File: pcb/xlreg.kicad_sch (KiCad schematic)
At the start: 12 parts, among them Q1076 2N7002a, Q1077 2N7002a, Q1078 2N7002a, Q1079 2N7002a, Q1080 2N7002a, Q1081 2N7002a, Q1082 2N7002a, Q1083 2N7002a, Q1084 2N7002a, Q1085 2N7002a

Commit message: XH/XL.
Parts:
- renumbered Q1076 to Q1009, Q1077 to Q1010, Q1078 to Q1011, Q1079 to Q1012, Q1080 to Q1013, Q1081 to Q1014, Q1082 to Q1015, Q1083 to Q1016, Q1084 to Q1017, Q1085 to Q1018, R466 to R441, R467 to R442
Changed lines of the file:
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@@
     (effects (font (size 1.27 1.27)) (justify left))
   )
-  (symbol (lib_id "power:VCC") (at 67.31 104.14 0) (unit 1)
-    (in_bom yes) (on_board yes)
-    (property "Reference" "#PWR0981" (id 0) (at 67.31 107.95 0)
+  (symbol (lib_id "power:VCC") (at 67.31 104.14 0)
+    (in_bom yes) (on_board yes)
+    (property "Reference" "#PWR0930" (id 0) (at 67.31 107.95 0)
       (effects (font (size 1.27 1.27)) hide)
     )
@@
     (pin "1")
   )
-  (symbol (lib_id "power:VCC") (at 135.89 46.99 0) (unit 1)
-    (in_bom yes) (on_board yes)
-    (property "Reference" "#PWR0973" (id 0) (at 135.89 50.8 0)
+  (symbol (lib_id "power:VCC") (at 135.89 46.99 0)
+    (in_bom yes) (on_board yes)
+    (property "Reference" "#PWR0922" (id 0) (at 135.89 50.8 0)
       (effects (font (size 1.27 1.27)) hide)
     )
@@
     (pin "1")
   )
-  (symbol (lib_id "power:GND") (at 67.31 87.63 0) (unit 1)
-    (in_bom yes) (on_board yes)
-    (property "Reference" "#PWR0976" (id 0) (at 67.31 93.98 0)
+  (symbol (lib_id "power:GND") (at 67.31 87.63 0)
+    (in_bom yes) (on_board yes)
+    (property "Reference" "#PWR0925" (id 0) (at 67.31 93.98 0)
       (effects (font (size 1.27 1.27)) hide)
     )
@@
     (pin "1")
   )
-  (symbol (lib_id "power:GND") (at 67.31 130.81 0) (unit 1)
-    (in_bom yes) (on_board yes)
-    (property "Reference" "#PWR0982" (id 0) (at 67.31 137.16 0)
+  (symbol (lib_id "power:GND") (at 67.31 130.81 0)
+    (in_bom yes) (on_board yes)
+    (property "Reference" "#PWR0931" (id 0) (at 67.31 137.16 0)
       (effects (font (size 1.27 1.27)) hide)
     )
@@
     (pin "1")
   )
-  (symbol (lib_id "power:GND") (at 93.98 95.25 0) (unit 1)
-    (in_bom yes) (on_board yes)
-    (property "Reference" "#PWR0977" (id 0) (at 93.98 101.6 0)
+  (symbol (lib_id "power:GND") (at 93.98 95.25 0)
+    (in_bom yes) (on_board yes)
+    (property "Reference" "#PWR0926" (id 0) (at 93.98 101.6 0)
       (effects (font (size 1.27 1.27)) hide)
     )
@@
     (pin "1")
   )
-  (symbol (lib_id "power:GND") (at 119.38 96.52 0) (unit 1)
-    (in_bom yes) (on_board yes)
-    (property "Reference" "#PWR0979" (id 0) (at 119.38 102.87 0)
+  (symbol (lib_id "power:GND") (at 119.38 96.52 0)
+    (in_bom yes) (on_board yes)
+    (property "Reference" "#PWR0928" (id 0) (at 119.38 102.87 0)
       (effects (font (size 1.27 1.27)) hide)
     )
@@
     (pin "1")
   )
-  (symbol (lib_id "power:GND") (at 148.59 96.52 0) (unit 1)
-    (in_bom yes) (on_board yes)
-    (property "Reference" "#PWR0980" (id 0) (at 148.59 102.87 0)
+  (symbol (lib_id "power:GND") (at 148.59 96.52 0)
+    (in_bom yes) (on_board yes)
+    (property "Reference" "#PWR0929" (id 0) (at 148.59 102.87 0)
       (effects (font (size 1.27 1.27)) hide)
     )
@@
     (pin "1")
   )
-  (symbol (lib_id "power:GND") (at 205.74 63.5 90) (unit 1)
-    (in_bom yes) (on_board yes)
-    (property "Reference" "#PWR0974" (id 0) (at 212.09 63.5 0)
+  (symbol (lib_id "power:GND") (at 205.74 63.5 90)
+    (in_bom yes) (on_board yes)
+    (property "Reference" "#PWR0923" (id 0) (at 212.09 63.5 0)
       (effects (font (size 1.27 1.27)) hide)
     )
@@
     (pin "1")
   )
-  (symbol (lib_id "power:GND") (at 205.74 68.58 90) (unit 1)
-    (in_bom yes) (on_board yes)
-    (property "Reference" "#PWR0975" (id 0) (at 212.09 68.58 0)
+  (symbol (lib_id "power:GND") (at 205.74 68.58 90)
+    (in_bom yes) (on_board yes)
+    (property "Reference" "#PWR0924" (id 0) (at 212.09 68.58 0)
       (effects (font (size 1.27 1.27)) hide)
     )
@@
     (pin "1")
   )
-  (symbol (lib_id "power:GND") (at 240.03 95.25 0) (unit 1)
-    (in_bom yes) (on_board yes)
-    (property "Reference" "#PWR0978" (id 0) (at 240.03 101.6 0)
+  (symbol (lib_id "power:GND") (at 240.03 95.25 0)
+    (in_bom yes) (on_board yes)
+    (property "Reference" "#PWR0927" (id 0) (at 240.03 101.6 0)
       (effects (font (size 1.27 1.27)) hide)
     )
@@
     (pin "1")
   )
-  (symbol (lib_id "Device:R") (at 67.31 107.95 0) (unit 1)
-    (in_bom yes) (on_board yes)
-    (property "Reference" "R467" (id 0) (at 69.088 106.7816 0)
+  (symbol (lib_id "Device:R") (at 67.31 107.95 0)
+    (in_bom yes) (on_board yes)
+    (property "Reference" "R442" (id 0) (at 69.088 106.7816 0)
       (effects (font (size 1.27 1.27)) (justify left))
     )
@@
     (pin "2")
   )
-  (symbol (lib_id "Device:R") (at 135.89 50.8 0) (unit 1)
-    (in_bom yes) (on_board yes)
-    (property "Reference" "R466" (id 0) (at 137.668 49.6316 0)
+  (symbol (lib_id "Device:R") (at 135.89 50.8 0)
+    (in_bom yes) (on_board yes)
+    (property "Reference" "R441" (id 0) (at 137.668 49.6316 0)
       (effects (font (size 1.27 1.27)) (justify left))
     )
@@
     (pin "2")
   )
-  (symbol (lib_id "Transistor_FET:2N7002") (at 64.77 82.55 0) (unit 1)
-    (in_bom yes) (on_board yes)
-    (property "Reference" "Q1080" (id 0) (at 70.0024 81.3816 0)
+  (symbol (lib_id "Transistor_FET:2N7002") (at 64.77 82.55 0)
+    (in_bom yes) (on_board yes)
+    (property "Reference" "Q1013" (id 0) (at 70.0024 81.3816 0)
       (effects (font (size 1.27 1.27)) (justify left))
     )
@@
     (pin "3")
   )
-  (symbol (lib_id "Transistor_FET:2N7002") (at 64.77 125.73 0) (unit 1)
-    (in_bom yes) (on_board yes)
-    (property "Reference" "Q1085" (id 0) (at 70.0024 124.5616 0)
+  (symbol (lib_id "Transistor_FET:2N7002") (at 64.77 125.73 0)
+    (in_bom yes) (on_board yes)
+    (property "Reference" "Q1018" (id 0) (at 70.0024 124.5616 0)
       (effects (font (size 1.27 1.27)) (justify left))
     )
@@
     (pin "3")
   )
-  (symbol (lib_id "Transistor_FET:2N7002") (at 91.44 80.01 0) (unit 1)
-    (in_bom yes) (on_board yes)
-    (property "Reference" "Q1076" (id 0) (at 96.6724 78.8416 0)
+  (symbol (lib_id "Transistor_FET:2N7002") (at 91.44 80.01 0)
+    (in_bom yes) (on_board yes)
+    (property "Reference" "Q1009" (id 0) (at 96.6724 78.8416 0)
       (effects (font (size 1.27 1.27)) (justify left))
     )
@@
     (pin "3")
   )
-  (symbol (lib_id "Transistor_FET:2N7002") (at 91.44 90.17 0) (unit 1)
-    (in_bom yes) (on_board yes)
-    (property "Reference" "Q1081" (id 0) (at 96.6724 89.0016 0)
+  (symbol (lib_id "Transistor_FET:2N7002") (at 91.44 90.17 0)
+    (in_bom yes) (on_board yes)
+    (property "Reference" "Q1014" (id 0) (at 96.6724 89.0016 0)
       (effects (font (size 1.27 1.27)) (justify left))
     )
@@
     (pin "3")
   )
-  (symbol (lib_id "Transistor_FET:2N7002") (at 116.84 81.28 0) (unit 1)
-    (in_bom yes) (on_board yes)
-    (property "Reference" "Q1078" (id 0) (at 122.0724 80.1116 0)
+  (symbol (lib_id "Transistor_FET:2N7002") (at 116.84 81.28 0)
+    (in_bom yes) (on_board yes)
+    (property "Reference" "Q1011" (id 0) (at 122.0724 80.1116 0)
       (effects (font (size 1.27 1.27)) (justify left))
     )
@@
     (pin "3")
   )
-  (symbol (lib_id "Transistor_FET:2N7002") (at 116.84 91.44 0) (unit 1)
-    (in_bom yes) (on_board yes)
-    (property "Reference" "Q1083" (id 0) (at 122.0724 90.2716 0)
+  (symbol (lib_id "Transistor_FET:2N7002") (at 116.84 91.44 0)
+    (in_bom yes) (on_board yes)
+    (property "Reference" "Q1016" (id 0) (at 122.0724 90.2716 0)
       (effects (font (size 1.27 1.27)) (justify left))
     )
@@
     (pin "3")
   )
-  (symbol (lib_id "Transistor_FET:2N7002") (at 146.05 81.28 0) (unit 1)
-    (in_bom yes) (on_board yes)
-    (property "Reference" "Q1079" (id 0) (at 151.2824 80.1116 0)
+  (symbol (lib_id "Transistor_FET:2N7002") (at 146.05 81.28 0)
+    (in_bom yes) (on_board yes)
+    (property "Reference" "Q1012" (id 0) (at 151.2824 80.1116 0)
       (effects (font (size 1.27 1.27)) (justify left))
     )
@@
     (pin "3")
   )
-  (symbol (lib_id "Transistor_FET:2N7002") (at 146.05 91.44 0) (unit 1)
-    (in_bom yes) (on_board yes)
-    (property "Reference" "Q1084" (id 0) (at 151.2824 90.2716 0)
+  (symbol (lib_id "Transistor_FET:2N7002") (at 146.05 91.44 0)
+    (in_bom yes) (on_board yes)
+    (property "Reference" "Q1017" (id 0) (at 151.2824 90.2716 0)
       (effects (font (size 1.27 1.27)) (justify left))
     )
@@
     (pin "3")
   )
-  (symbol (lib_id "Transistor_FET:2N7002") (at 237.49 80.01 0) (unit 1)
-    (in_bom yes) (on_board yes)
-    (property "Reference" "Q1077" (id 0) (at 242.7224 78.8416 0)
+  (symbol (lib_id "Transistor_FET:2N7002") (at 237.49 80.01 0)
+    (in_bom yes) (on_board yes)
+    (property "Reference" "Q1010" (id 0) (at 242.7224 78.8416 0)
       (effects (font (size 1.27 1.27)) (justify left))
     )
@@
     (pin "3")
   )
-  (symbol (lib_id "Transistor_FET:2N7002") (at 237.49 90.17 0) (unit 1)
-    (in_bom yes) (on_board yes)
-    (property "Reference" "Q1082" (id 0) (at 242.7224 89.0016 0)
-      (effects (font (size 1.27 1.27)) (justify left))
-    )
+  (symbol (lib_id "Transistor_FET:2N7002") (at 237.49 90.17 0)
+    (in_bom yes) (on_board yes)
+    (property "Reference" "Q1015" (id 0) (at 242.7224 89.0016 0)
+      (effects (font (size 1.27 1.27)) (justify left))
+    )

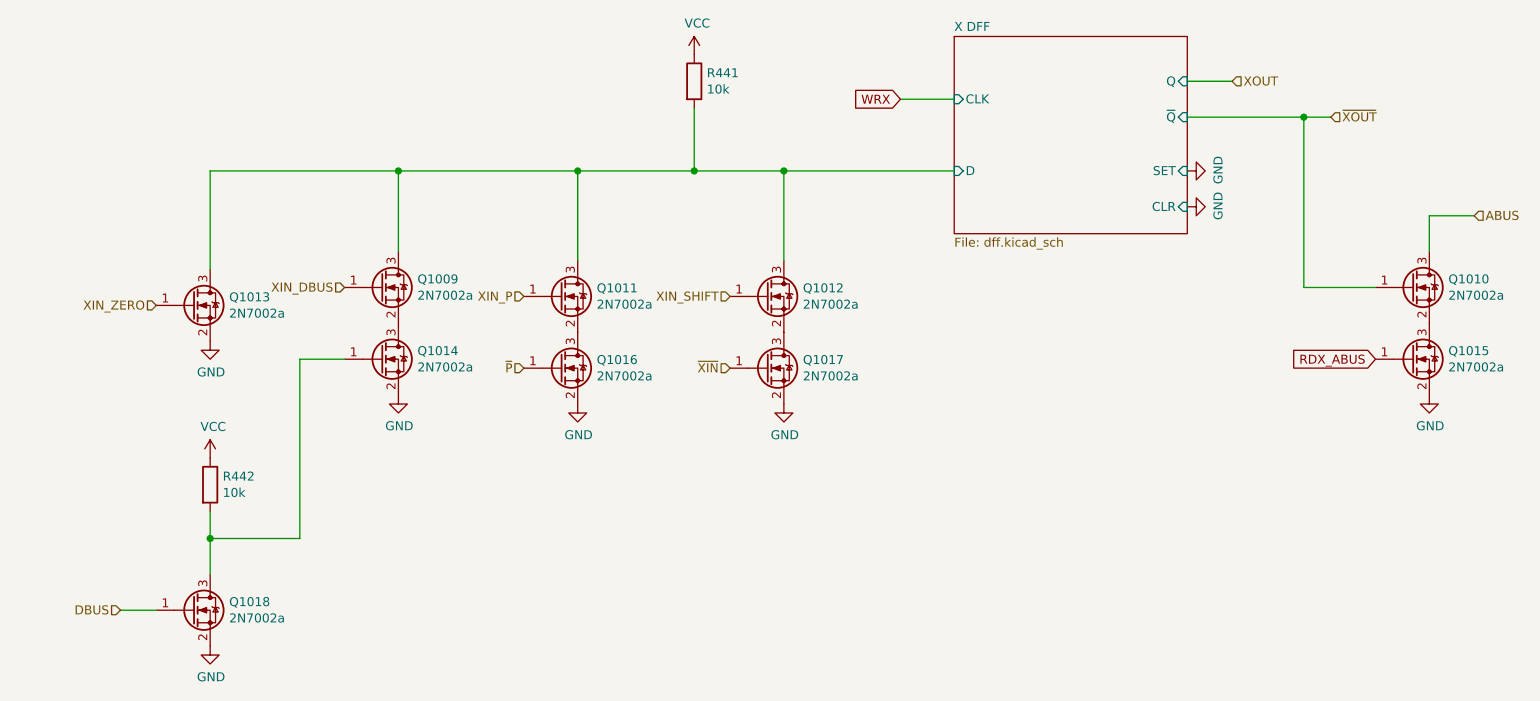
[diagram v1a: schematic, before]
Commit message: Fewer transistors.
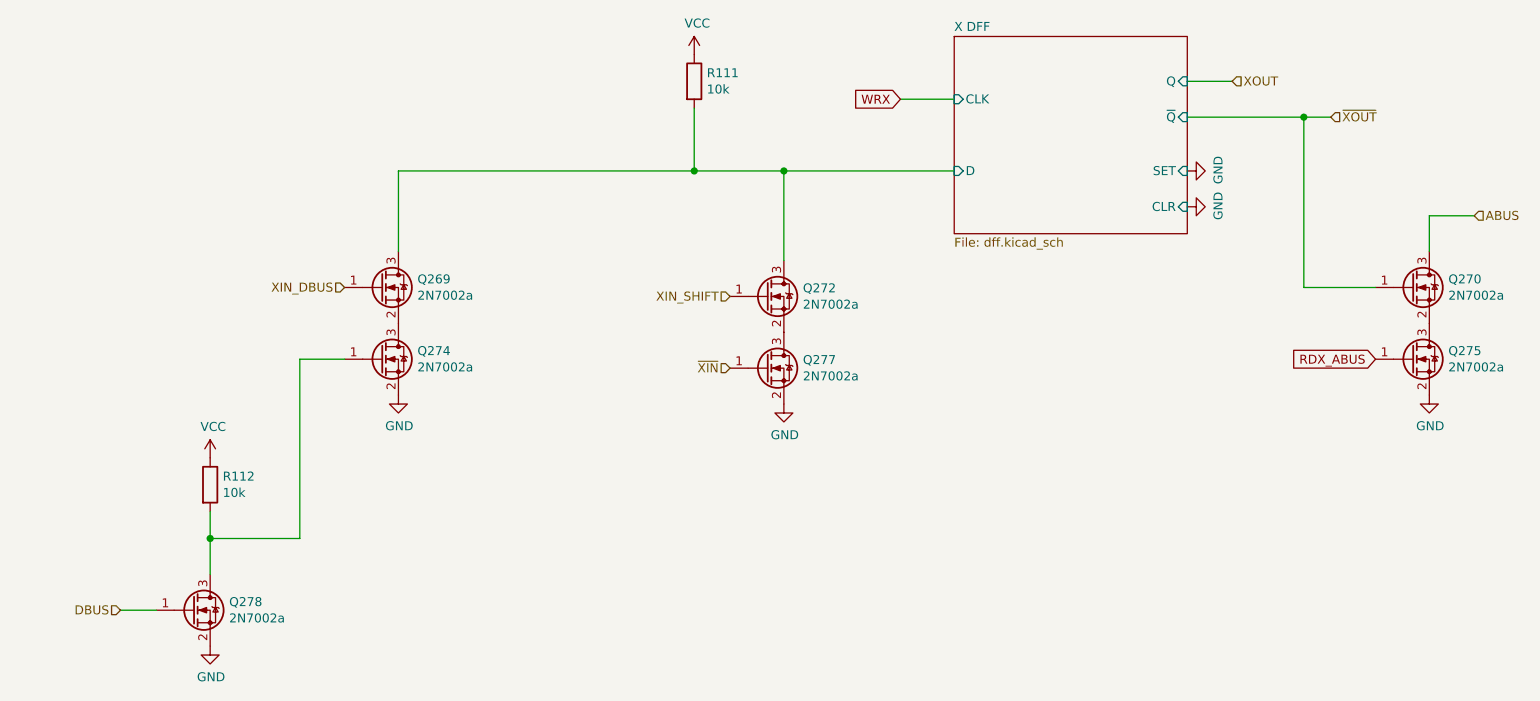
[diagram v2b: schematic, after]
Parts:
- removed Q1011, Q1013, Q1016: 2N7002a, Package_TO_SOT_SMD:SOT-23, symbol Transistor_FET:2N7002
- renumbered Q1009 to Q269, Q1010 to Q270, Q1012 to Q272, Q1014 to Q274, Q1015 to Q275, Q1017 to Q277, Q1018 to Q278, R441 to R111, R442 to R112

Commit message: Relink.
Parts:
- renumbered Q269 to Q1076, Q270 to Q1077, Q272 to Q1079, Q274 to Q1081, Q275 to Q1082, Q277 to Q1084, Q278 to Q1085, R111 to R466, R112 to R467
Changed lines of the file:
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@@
   (symbol (lib_id "Device:R") (at 67.31 107.95 0)
     (in_bom yes) (on_board yes)
-    (property "Reference" "R112" (id 0) (at 69.088 106.7816 0)
+    (property "Reference" "R467" (id 0) (at 69.088 106.7816 0)
       (effects (font (size 1.27 1.27)) (justify left))
     )
@@
   (symbol (lib_id "Device:R") (at 135.89 50.8 0)
     (in_bom yes) (on_board yes)
-    (property "Reference" "R111" (id 0) (at 137.668 49.6316 0)
+    (property "Reference" "R466" (id 0) (at 137.668 49.6316 0)
       (effects (font (size 1.27 1.27)) (justify left))
     )
@@
   (symbol (lib_id "Transistor_FET:2N7002") (at 64.77 125.73 0)
     (in_bom yes) (on_board yes)
-    (property "Reference" "Q278" (id 0) (at 70.0024 124.5616 0)
+    (property "Reference" "Q1085" (id 0) (at 70.0024 124.5616 0)
       (effects (font (size 1.27 1.27)) (justify left))
     )
@@
   (symbol (lib_id "Transistor_FET:2N7002") (at 91.44 80.01 0)
     (in_bom yes) (on_board yes)
-    (property "Reference" "Q269" (id 0) (at 96.6724 78.8416 0)
+    (property "Reference" "Q1076" (id 0) (at 96.6724 78.8416 0)
       (effects (font (size 1.27 1.27)) (justify left))
     )
@@
   (symbol (lib_id "Transistor_FET:2N7002") (at 91.44 90.17 0)
     (in_bom yes) (on_board yes)
-    (property "Reference" "Q274" (id 0) (at 96.6724 89.0016 0)
+    (property "Reference" "Q1081" (id 0) (at 96.6724 89.0016 0)
       (effects (font (size 1.27 1.27)) (justify left))
     )
@@
   (symbol (lib_id "Transistor_FET:2N7002") (at 146.05 81.28 0)
     (in_bom yes) (on_board yes)
-    (property "Reference" "Q272" (id 0) (at 151.2824 80.1116 0)
+    (property "Reference" "Q1079" (id 0) (at 151.2824 80.1116 0)
       (effects (font (size 1.27 1.27)) (justify left))
     )
@@
   (symbol (lib_id "Transistor_FET:2N7002") (at 146.05 91.44 0)
     (in_bom yes) (on_board yes)
-    (property "Reference" "Q277" (id 0) (at 151.2824 90.2716 0)
+    (property "Reference" "Q1084" (id 0) (at 151.2824 90.2716 0)
       (effects (font (size 1.27 1.27)) (justify left))
     )
@@
   (symbol (lib_id "Transistor_FET:2N7002") (at 237.49 80.01 0)
     (in_bom yes) (on_board yes)
-    (property "Reference" "Q270" (id 0) (at 242.7224 78.8416 0)
+    (property "Reference" "Q1077" (id 0) (at 242.7224 78.8416 0)
       (effects (font (size 1.27 1.27)) (justify left))
     )
@@
   (symbol (lib_id "Transistor_FET:2N7002") (at 237.49 90.17 0)
     (in_bom yes) (on_board yes)
-    (property "Reference" "Q275" (id 0) (at 242.7224 89.0016 0)
+    (property "Reference" "Q1082" (id 0) (at 242.7224 89.0016 0)
       (effects (font (size 1.27 1.27)) (justify left))
     )

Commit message: Fix UUIDs.
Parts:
- renumbered Q1076 to Q1058, Q1077 to Q1059, Q1079 to Q1060, Q1081 to Q1061, Q1082 to Q1062, Q1084 to Q1063, Q1085 to Q1064
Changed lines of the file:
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@@
   (symbol (lib_id "power:VCC") (at 67.31 104.14 0)
     (in_bom yes) (on_board yes)
-    (property "Reference" "#PWR0981" (id 0) (at 67.31 107.95 0)
+    (property "Reference" "#PWR0953" (id 0) (at 67.31 107.95 0)
       (effects (font (size 1.27 1.27)) hide)
     )
@@
   (symbol (lib_id "power:VCC") (at 135.89 46.99 0)
     (in_bom yes) (on_board yes)
-    (property "Reference" "#PWR0973" (id 0) (at 135.89 50.8 0)
+    (property "Reference" "#PWR0947" (id 0) (at 135.89 50.8 0)
       (effects (font (size 1.27 1.27)) hide)
     )
@@
   (symbol (lib_id "power:GND") (at 67.31 130.81 0)
     (in_bom yes) (on_board yes)
-    (property "Reference" "#PWR0982" (id 0) (at 67.31 137.16 0)
+    (property "Reference" "#PWR0954" (id 0) (at 67.31 137.16 0)
       (effects (font (size 1.27 1.27)) hide)
     )
@@
   (symbol (lib_id "power:GND") (at 93.98 95.25 0)
     (in_bom yes) (on_board yes)
-    (property "Reference" "#PWR0977" (id 0) (at 93.98 101.6 0)
+    (property "Reference" "#PWR0950" (id 0) (at 93.98 101.6 0)
       (effects (font (size 1.27 1.27)) hide)
     )
@@
   (symbol (lib_id "power:GND") (at 148.59 96.52 0)
     (in_bom yes) (on_board yes)
-    (property "Reference" "#PWR0980" (id 0) (at 148.59 102.87 0)
+    (property "Reference" "#PWR0952" (id 0) (at 148.59 102.87 0)
       (effects (font (size 1.27 1.27)) hide)
     )
@@
   (symbol (lib_id "power:GND") (at 205.74 63.5 90)
     (in_bom yes) (on_board yes)
-    (property "Reference" "#PWR0974" (id 0) (at 212.09 63.5 0)
+    (property "Reference" "#PWR0948" (id 0) (at 212.09 63.5 0)
       (effects (font (size 1.27 1.27)) hide)
     )
@@
   (symbol (lib_id "power:GND") (at 205.74 68.58 90)
     (in_bom yes) (on_board yes)
-    (property "Reference" "#PWR0975" (id 0) (at 212.09 68.58 0)
+    (property "Reference" "#PWR0949" (id 0) (at 212.09 68.58 0)
       (effects (font (size 1.27 1.27)) hide)
     )
@@
   (symbol (lib_id "power:GND") (at 240.03 95.25 0)
     (in_bom yes) (on_board yes)
-    (property "Reference" "#PWR0978" (id 0) (at 240.03 101.6 0)
+    (property "Reference" "#PWR0951" (id 0) (at 240.03 101.6 0)
       (effects (font (size 1.27 1.27)) hide)
     )
@@
   (symbol (lib_id "Transistor_FET:2N7002") (at 64.77 125.73 0)
     (in_bom yes) (on_board yes)
-    (property "Reference" "Q1085" (id 0) (at 70.0024 124.5616 0)
+    (property "Reference" "Q1064" (id 0) (at 70.0024 124.5616 0)
       (effects (font (size 1.27 1.27)) (justify left))
     )
@@
   (symbol (lib_id "Transistor_FET:2N7002") (at 91.44 80.01 0)
     (in_bom yes) (on_board yes)
-    (property "Reference" "Q1076" (id 0) (at 96.6724 78.8416 0)
+    (property "Reference" "Q1058" (id 0) (at 96.6724 78.8416 0)
       (effects (font (size 1.27 1.27)) (justify left))
     )
@@
   (symbol (lib_id "Transistor_FET:2N7002") (at 91.44 90.17 0)
     (in_bom yes) (on_board yes)
-    (property "Reference" "Q1081" (id 0) (at 96.6724 89.0016 0)
+    (property "Reference" "Q1061" (id 0) (at 96.6724 89.0016 0)
       (effects (font (size 1.27 1.27)) (justify left))
     )
@@
   (symbol (lib_id "Transistor_FET:2N7002") (at 146.05 81.28 0)
     (in_bom yes) (on_board yes)
-    (property "Reference" "Q1079" (id 0) (at 151.2824 80.1116 0)
+    (property "Reference" "Q1060" (id 0) (at 151.2824 80.1116 0)
       (effects (font (size 1.27 1.27)) (justify left))
     )
@@
   (symbol (lib_id "Transistor_FET:2N7002") (at 146.05 91.44 0)
     (in_bom yes) (on_board yes)
-    (property "Reference" "Q1084" (id 0) (at 151.2824 90.2716 0)
+    (property "Reference" "Q1063" (id 0) (at 151.2824 90.2716 0)
       (effects (font (size 1.27 1.27)) (justify left))
     )
@@
   (symbol (lib_id "Transistor_FET:2N7002") (at 237.49 80.01 0)
     (in_bom yes) (on_board yes)
-    (property "Reference" "Q1077" (id 0) (at 242.7224 78.8416 0)
+    (property "Reference" "Q1059" (id 0) (at 242.7224 78.8416 0)
       (effects (font (size 1.27 1.27)) (justify left))
     )
@@
   (symbol (lib_id "Transistor_FET:2N7002") (at 237.49 90.17 0)
     (in_bom yes) (on_board yes)
-    (property "Reference" "Q1082" (id 0) (at 242.7224 89.0016 0)
-      (effects (font (size 1.27 1.27)) (justify left))
-    )
+    (property "Reference" "Q1062" (id 0) (at 242.7224 89.0016 0)
+      (effects (font (size 1.27 1.27)) (justify left))
+    )
